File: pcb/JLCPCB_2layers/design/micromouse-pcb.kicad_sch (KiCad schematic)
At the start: 130 parts, among them J1 BATT_IN_2S, J10 BATT_IN_XT60 (parallel option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, J5 MOTOR_A_N20_ENCODER, J6 MOTOR_B_N20_ENCODER, J7 USB-C rear (GCT USB4105; VBUS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, J9 BALANCE_2S, Q1 Q_PMOS reverse guard (DMP3098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, Q16 BSS138 (real part; Q_NMOS_GSD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, Q17 BSS138 (real part; Q_NMOS_GSD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, Q18 BSS138 (real part; Q_NMOS_GSD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, Q19 BSS84 (PMOS indicator driver;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, Q2 PT334-6B (5mm filtered PT; LO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, Q20 BSS84 (PMOS indicator driver;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, Q21 BSS84 (PMOS indicator driver;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, Q22 BSS84 (PMOS indicator driver;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, Q23 BSS84 (PMOS indicator driver;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, Q24 BSS84 (PMOS indicator driver;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, Q3 PT334-6B (5mm filtered PT; LO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, Q34 MMBT2222A (buzzer low-side dr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, Q4 PT334-6B (5mm filtered PT; LO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, Q5 PT334-6B (5mm filtered PT; LO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, Q6 PT334-6B (5mm filtered PT; LO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, Q7 PT334-6B (5mm filtered PT; LO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, SW1 BTN_A (start / BOOT), SW2 RESET, SW3 BTN_B, SW4 BTN_C, SW5 PWR ALL (PCM12SMTR slide; sli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, SW6 PWR MOTORS (PCM12SMTR slide; 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, U1 AP63203WU-7 (fixed 3.3V 2A bu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, U2 TB6612FNG, U3 ESP32-S3-WROOM-1-N8R2 (quad P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, U6 USBLC6-2SC6 (SOT-23-6; 2P6 ba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, U7 TPS54302DDCR (6.0V/3A motor b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, U8 BNO055 (9-axis IMU + fusion; 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

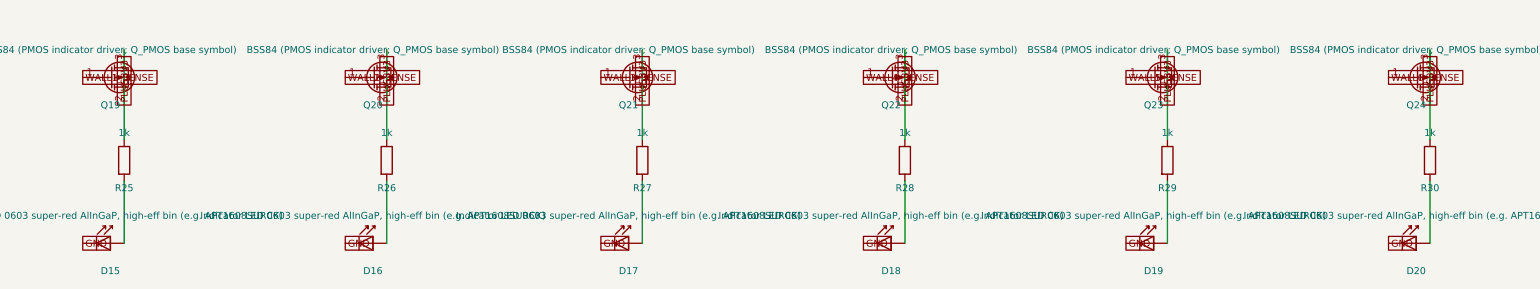
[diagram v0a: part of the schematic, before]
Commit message: 2-layer JLCPCB: initial placement + render (for review)
build_pcb.py adapted for the 2-layer part set:
- 2 copper layers (was 4); inner GND/3V3 planes replaced by solid GND pours on
  both outer layers (power rails routed as traces in the routing phase).
- Skip-missing placement wrapper drops the removed parts (line array LS1-8,
  line indicators, mux U4, JTAG J8) automatically; retained parts keep their
  4-layer positions.
- Restored the buzzer cluster (BZ1/Q34/D29/R81) + XT60 J10 placements (they were
  hand-placed in the frozen 4-layer board, never in build_pcb.py).
- Placed the new power/status/RGB LEDs (D30/D31/D32 + R82/R83/C31), provisional.
- THT hand-solder-margin gate downgraded to advisory (board is JLC machine-
  assembled); the one flagged pair (SW2<->R12, 2.04mm) will be nudged clear in
  refinement.

Board: 2 layers, 137 footprints, all 398 pins mapped, no courtyard overlaps,
bodies inside outline. Renders in images/placement_{top,bottom}.png.

Refinement next: motor connectors J5/J6 symmetric, J9 balance "OPTIONAL" silk,
confirm side indicators clear of IR beams, ALL refdes on silk, route to DRC 0/0.

Co-Authored-By: Claude Fable 5 <noreply@anthropic.com>
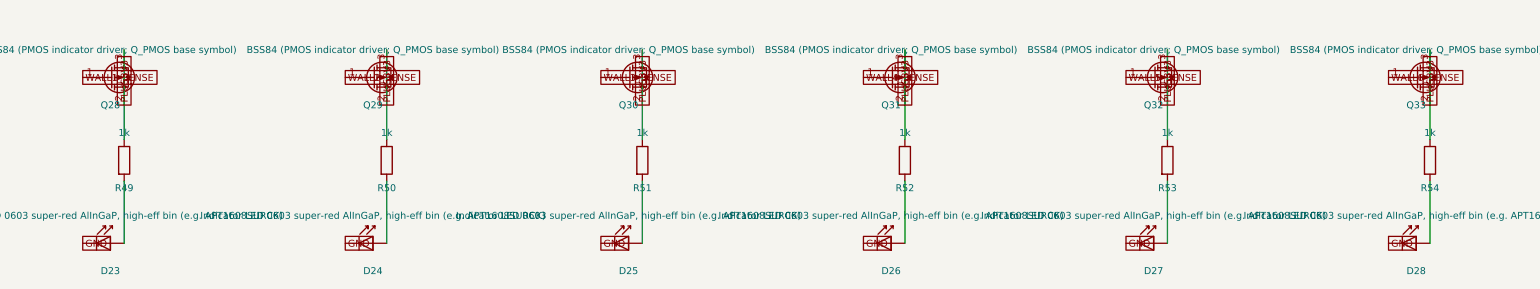
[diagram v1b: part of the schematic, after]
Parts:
- removed D15, D16, D17, D18, D19, D20: Indicator LED 0603 super-red AlInGaP, high-eff bi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, LED_SMD:LED_0603_1608Metric, symbol LED:LD271
- removed Q19, Q20, Q21, Q22, Q23, Q24: BSS84 (PMOS indicator driver; Q_PMOS base symbol), Package_TO_SOT_SMD:SOT-23, symbol Transistor_FET:Q_PMOS_GSD
- removed R25, R26, R27, R28, R29, R30: 1k, Resistor_SMD:R_0805_2012Metric, symbol Device:R
- added D23, D24, D25, D26, D27, D28: Indicator LED 0603 super-red AlInGaP, high-eff bi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, LED_SMD:LED_0603_1608Metric, symbol LED:LD271
- added Q28, Q29, Q30, Q31, Q32, Q33: BSS84 (PMOS indicator driver; Q_PMOS base symbol), Package_TO_SOT_SMD:SOT-23, symbol Transistor_FET:Q_PMOS_GSD
- added R49, R50, R51, R52, R53, R54: 1k, Resistor_SMD:R_0805_2012Metric, symbol Device:R
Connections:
- net GND: now also D23.1 (K), D24.1 (K), D25.1 (K), D26.1 (K), D27.1 (K), D28.1 (K), Q28.1 (G), Q28.2 (S), Q28.3 (D), Q29.1 (G), Q29.2 (S), Q29.3 (D), Q30.1 (G), Q30.2 (S), Q30.3 (D), Q31.1 (G), Q31.2 (S), Q31.3 (D), Q32.1 (G), Q32.2 (S), Q32.3 (D), Q33.1 (G), Q33.2 (S), Q33.3 (D), R49.1, R50.1, R51.1, R52.1, R53.1, R54.1
- new net: D25.2 (A), R51.2
- new net: D27.2 (A), R53.2
- new net: D26.2 (A), R52.2
- new net: D28.2 (A), R54.2
- new net: D24.2 (A), R50.2
- new net: D23.2 (A), R49.2

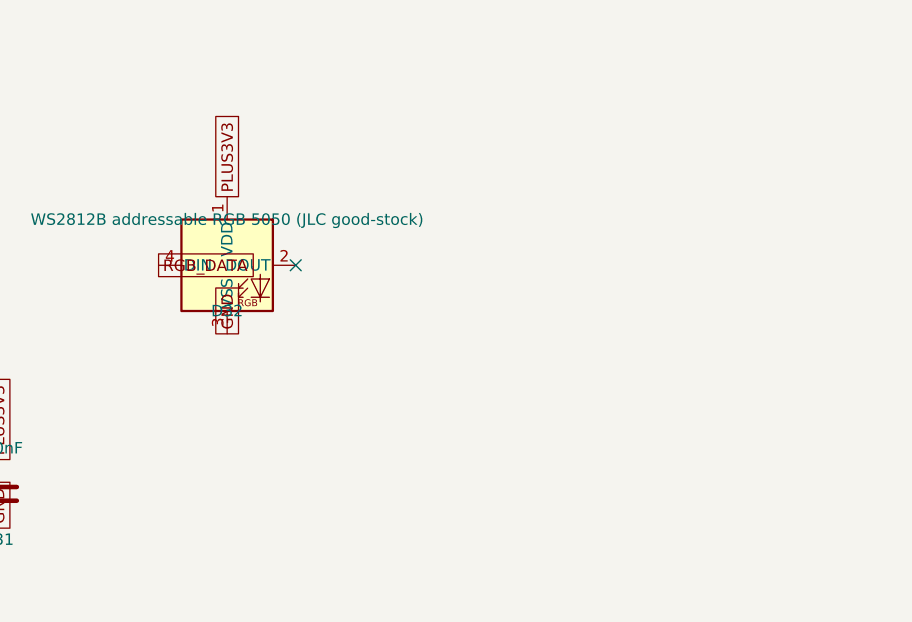
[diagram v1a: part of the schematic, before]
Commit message: 2-layer: add motor-power LED (D33), shift ESP off the left wheel
- New motor-rail indicator LED D33 (+R84): ON when SW6 is on and VM_6V is up
  (VM_6V -> 1k -> LED -> GND). Grouped with D30 (power) / D31 (status) at the
  rear by RST as three labeled indicators.
- ESP U3 shifted +2.75mm toward centre (35.25 -> 38.0) with its antenna notch
  (board_geom ANT_NOTCH) + ribbon keepout: left-wheel clearance 0.75mm -> ~3.5mm
  (max shift the rear-centre buzzer allows without relocating it).
- ESP decoupling C8/C10 moved to the bottom face under U3 (buzzer blocks the
  top-face gap). No courtyard overlaps; ERC 0; 138 components.

Renders updated. Full dead-centre ESP would need relocating the buzzer cluster
(rear-centre is packed) -- offered to the user.

Co-Authored-By: Claude Fable 5 <noreply@anthropic.com>
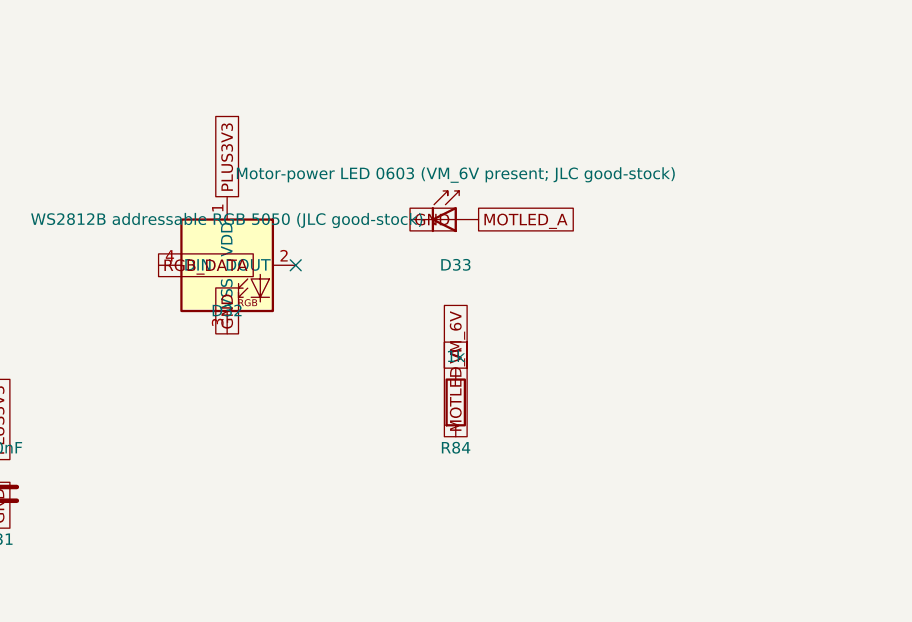
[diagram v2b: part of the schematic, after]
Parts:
- added D33: Motor-power LED 0603 (VM_6V present; JLC good-sto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, LED_SMD:LED_0603_1608Metric, symbol LED:LD271
- added R84: 1k, Resistor_SMD:R_0805_2012Metric, symbol Device:R
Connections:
- net GND: now also D33.1 (K)
- net VM_6V: now also R84.1
- new net MOTLED_A: D33.2 (A), R84.2

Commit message: 2-layer: user placement review + motor-bay routing + full route (0 err / 0 parity)
Extensive user-directed placement/mechanical review, then routed to a
manufacturable state:

Placement (user render review):
- Diagonal IR emitters D3/D4 restored to the 45-deg cluster + detectors Q4/Q5
  rotated to align (reverts the 1297b67 center-pull); shifted up 2mm to clear
  the side detectors within the front edge-gap.
- Obstruction sensor pull-ups R13-R20 moved behind/inboard of their sensors,
  off the beam path.
- C30 (6.3x7.7mm electrolytic) moved OFF the bottom layer -> TOP by R6/R7:
  a 7.7mm part on the bottom would drag on the maze floor. Bottom is now all
  low-profile SMD. Kept clear of the motor + mount.
- J6 made mirror-symmetric to J5 (rot 180) so it clears the H3 mount hole.
- BATT label moved to the battery connectors; PWR/MOT switch labels lifted off
  the switch bodies (were unreadable).

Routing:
- USER insight: opened the motor-bay TOP space (the F.Cu motor keepout blocked
  Freerouting from the top under the motors). Motors have no copper pads and sit
  on standoffs, so top routing + top GND pour there are fine. MOT1 now 19 / MOT2
  16 top tracks; top pour fills the bays -> less GND fragmentation.
- Hard U3-escape nets pre-routed on the empty board; Freerouting completes 100%
  of signal (0 unrouted, score 994.80).
- GND pour stitched with vias (smart + chained, deduped) to ratsnest 5. The
  remaining 5 are non-critical: 2 redundant IMU (BNO055) ground pads (the IMU is
  grounded via its 4 other GND pads) + 3 floating pour slivers. Every critical
  ground connects.

Verify: 0 DRC errors, 0 schematic parity, silk finalized (refdes -> fab),
check_pins 28/28, ERC 0. Renders refreshed (top + bottom, placement + routed).

Co-Authored-By: Claude Opus 4.8 (1M context) <noreply@anthropic.com>
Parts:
- removed C19: 100nF, Capacitor_SMD:C_0805_2012Metric, symbol Device:C
- removed J9: BALANCE_2S, Connector_JST:JST_XH_B3B-XH-A_1x03_P2.50mm_Vertical, symbol Connector_Generic:Conn_01x03
- removed R75, R76: 100k, Resistor_SMD:R_0805_2012Metric, symbol Device:R
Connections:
- net GND: now also J7.A5 (CC1), R12.1; no longer U3.12 (IO8)
- no-connect marks 13 -> 14
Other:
- note added: "VBAT_SENSE = pack (0-8.4V) x 39/139 <= 2.36V on ADC1 IO7 (direct). VBUS_SENSE = 5V x 15/25 <= 3.15V on IO9. PACK-LEVEL monitoring only (per-cell/balance removed). Firmware cutoff: 6.6V pack floor (3.3V/cell avg); the 6V motor rail stays in regulation across the 6.6-8.4V window."
- note removed: "VBAT_SENSE = pack (0-8.4V) x 39/139 <= 2.36V; BAT_MID_SENSE = cell-1 (0-4.2V) x 1/2 <= 2.1V. Both + VBUS_SENSE read through mux channels Y8/Y9/Y10 (ADC1 IO7). Firmware cutoff: 3.3V/cell (either cell) = 6.6V pack floor; the 6V rail is in regulation across that window."

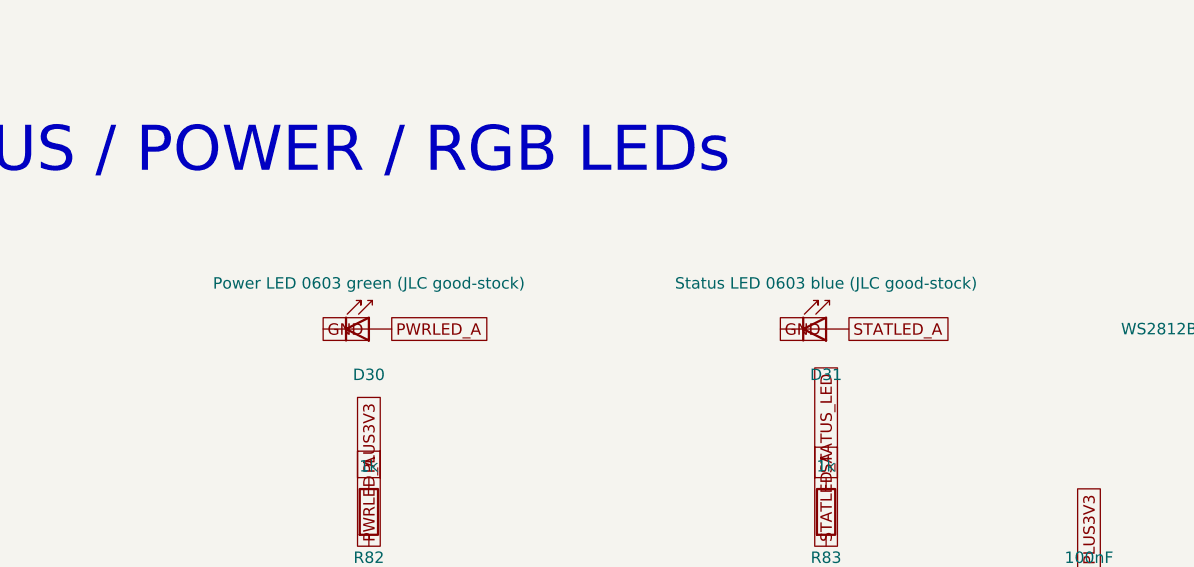
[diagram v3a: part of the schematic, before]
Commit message: 2-layer BOM: stocked JLC parts for the LED + buzzer lines (user assembly review)
From the user's JLCPCB BOM-matching screenshots:

- Indicator LEDs (D23-D28, D30, D31, D33): the multi-line match warning is
  by-design (one red 0603 LED reused across all indicator roles), BUT the
  matched C5875723 has 0 in JLC's assembly pool (LCSC-retail-only). SUB to
  C2286 / KT-0603R -- JLC Basic tier, 3.59M stock (2026-07-21), 0603 pad- and
  Vf-compatible (1.8-2.4V), 300mcd; series resistors unchanged. Also fixed the
  stale "green"/"blue" Value labels at the schematic source: every indicator
  is physically RED (design reuses the wall-indicator part).
- Buzzer BZ1: C3811795 (JLC-consigned listing) hit Inventory shortage. The
  in-stock row is the SAME MPN (CUI CMT-8504-100-SMT-TR) under the regular
  LCSC listing C22359707 (104 stock) -- exact drop-in, verified not a
  substitute. BOM now carries C22359707.

Propagated: schematic + netlist regenerated, ERC 0, check_pins 28/28,
sim_imu PASS, sync_board_meta (2 values), DRC 0 errors / 0 parity,
export_fab ALL GATES, JLC package re-exported + validate_jlc_files ALL PASS.
Board copper untouched (diff = 2 value strings).

Co-Authored-By: Claude Fable 5 <noreply@anthropic.com>
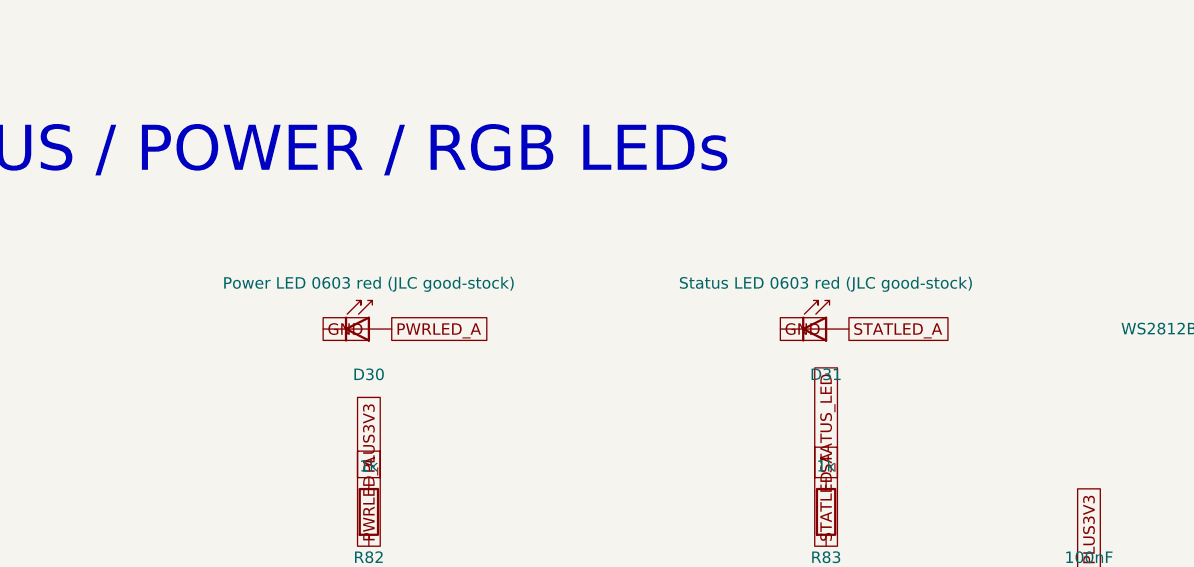
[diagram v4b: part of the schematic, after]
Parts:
- D30: value Power LED 0603 green (JLC good-stock) -> Power LED 0603 red (JLC good-stock)
- D31: value Status LED 0603 blue (JLC good-stock) -> Status LED 0603 red (JLC good-stock)

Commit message: 2-layer PRODUCTION: final JLCPCB + Lion Circuits release (wall sensors only)
Production-ready release for the 2-layer micromouse board (wall sensors
only, no line array/mux/JTAG): U8 (IMU) + U2 (motor driver) flipped to
the bottom layer, full clean-slate Freerouting re-route, GND pour
fragment bridging, BOM duplicate-part merge, and DRC cleanup (0 errors,
0 warnings). Includes matching production folders for both JLCPCB and
Lion Circuits (BOM, CPL, gerbers).

Co-Authored-By: Claude Sonnet 5 <noreply@anthropic.com>
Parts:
- D32: MPN WS2812B -> XL-5050RGBC-WS2812B; Manufacturer Worldsemi -> Xinglight
- F1: MPN MINISMDC350F/16-2 -> MINISMDC260F/16-2
- R10, R11, R55, R6, R65, R67, R7, R79, R8, R80, R9: MPN RC0805FR-0710KL -> WR08X1002FTL; Manufacturer Yageo -> Walsin
- SW1: footprint Button_Switch_THT:SW_PUSH_6mm -> Button_Switch_SMD:SW_Push_1P1T_NO_CK_KMR2; MPN PTS645VL582LFS -> KMR221NGLFS
- SW2: value RESET -> BTN_B; footprint Button_Switch_THT:SW_PUSH_6mm -> Button_Switch_SMD:SW_Push_1P1T_NO_CK_KMR2; MPN PTS645VL582LFS -> KMR221NGLFS
- SW3: value BTN_B -> BTN_C; footprint Button_Switch_THT:SW_PUSH_6mm -> Button_Switch_SMD:SW_Push_1P1T_NO_CK_KMR2; MPN PTS645VL582LFS -> KMR221NGLFS
- SW4: value BTN_C -> RESET; footprint Button_Switch_THT:SW_PUSH_6mm -> Button_Switch_SMD:SW_Push_1P1T_NO_CK_KMR2; MPN PTS645VL582LFS -> KMR221NGLFS
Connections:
- net ESP_EN: now also SW4.1; no longer SW2.1
- net USER_BTN2: now also SW2.1; no longer SW3.1
- net USER_BTN3: now also SW3.1; no longer SW4.1
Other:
- note added: "Buttons are lettered on the silkscreen: A=SW1, B=SW2, C=SW3, RST=SW4. SW1/A = USER_BTN on IO0: start-run button AND the BOOT strap (hold A, tap RST -> ROM download mode). External 10k pull-up R10 keeps the strap solid. SW2/SW3 = USER_BTN2/3 on IO35/IO36 (menu/select UX): active-low, firmware enables the internal pull-ups -- no external resistors. NOTE: on octal-PSRAM (-R8) modules IO35/36 do not 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"
- note removed: "Buttons are lettered on the silkscreen: A=SW1, B=SW3, C=SW4, RST=SW2. SW1/A = USER_BTN on IO0: start-run button AND the BOOT strap (hold A, tap RST -> ROM download mode). External 10k pull-up R10 keeps the strap solid. SW3/SW4 = USER_BTN2/3 on IO35/IO36 (menu/select UX): active-low, firmware enables the internal pull-ups -- no external resistors. NOTE: on octal-PSRAM (-R8) modules IO35/36 do not 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"
